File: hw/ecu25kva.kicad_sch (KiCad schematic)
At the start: 0 parts

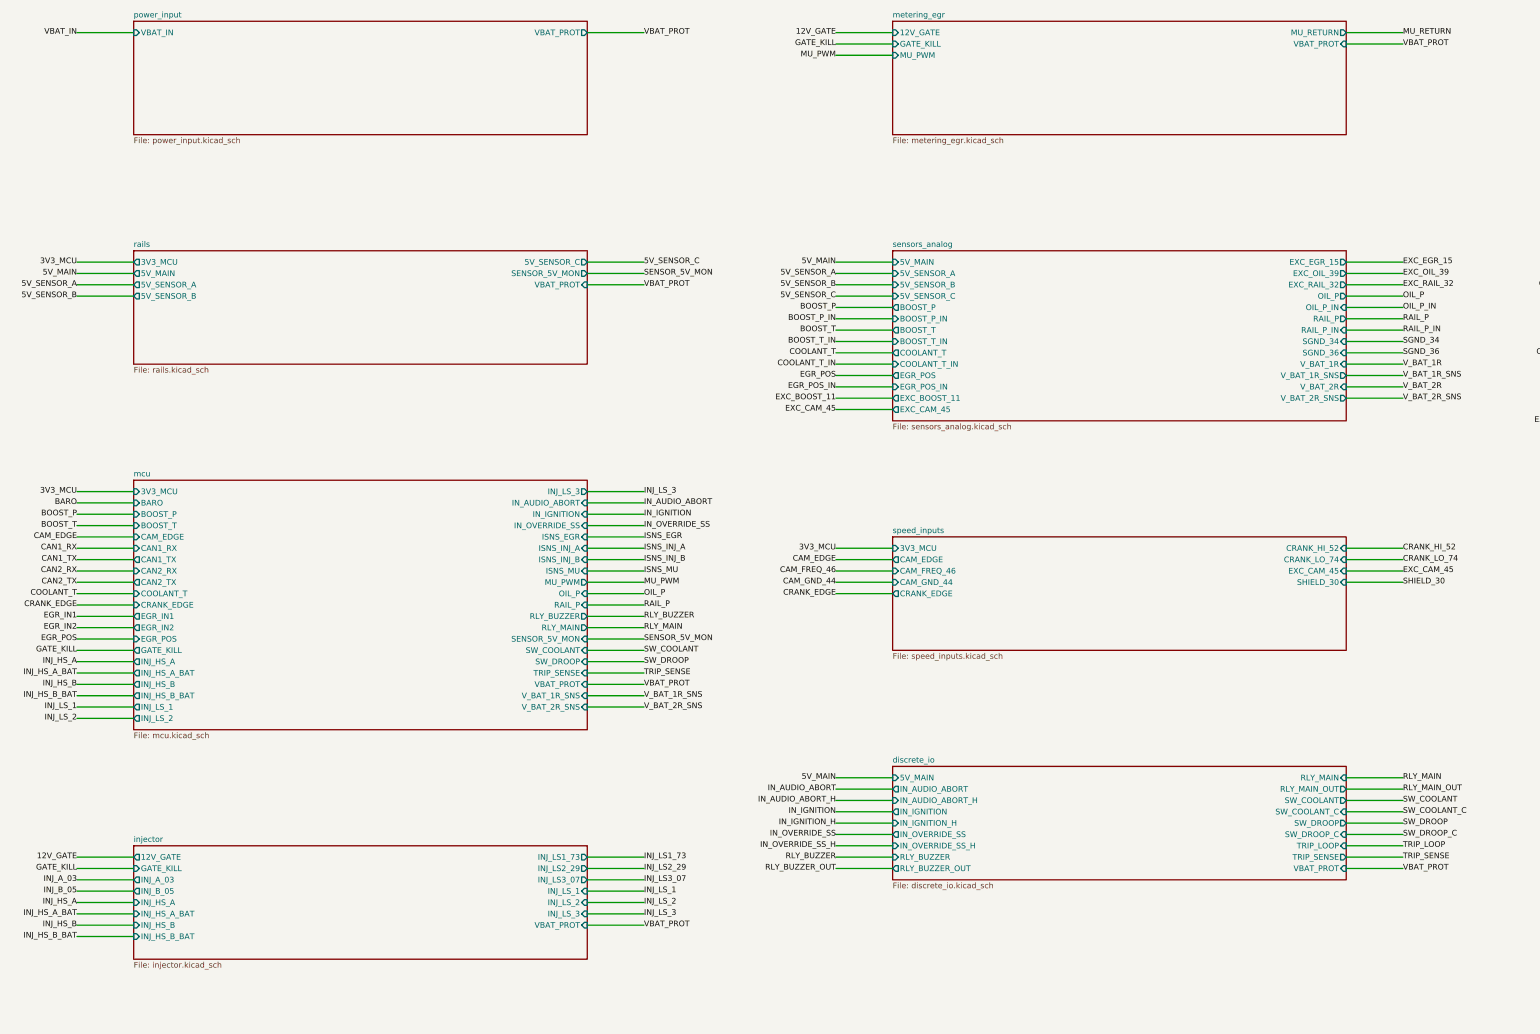
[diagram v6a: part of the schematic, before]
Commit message: Choose the current-sense amplifiers: INA181A1-Q1 on all three channels
TI SLYS018F, retrieved and text-extracted. VCM -0.2 V to 26 V, so it
sits across a ground-referenced shunt; gain 20; 350 kHz; +/-150 uV
offset at VCM = 0.

One part, one gain, three channels, and the gain is set for the
injector: 5 mOhm x 18 A x 20 = 1.80 V at the peak, 1.00 V at the 10 A
hold, leaving headroom to 3.28 V -- so a fault current up to 32.8 A is
MEASURED rather than clipped, which is what an overcurrent check needs.
The metering channel takes the same gain and reads its 0.675 A setpoint
at 675 mV, 844 counts.

Supplied from 3V3_MCU, which makes the output ADC-safe by construction:
it cannot swing above VS - 0.02 V, so these three channels need no
3.3 V zener at the MCU pin, unlike every channel on sensors_analog.

Closes MU-ISENSE's open half -- that tag specified the 50 mOhm shunt and
said the amplifier was not optional. The Kelvin-tap layout requirement
is carried in each amplifier's own field.

Also redrawn: the metering FET, placed at rot=270 since 20 September.
At 270 the drain and source sit side by side and every wire to a rail
above or below comes out diagonal -- the same drawing bug the injector
sheet had and fixed first. The netlist was always right; the page was
not.

Open ends 12 -> 9. 24/24 blocks, 24/24 netlist checks, 36 supply pins
all decoupled.

Co-Authored-By: Claude Opus 5 <noreply@anthropic.com>
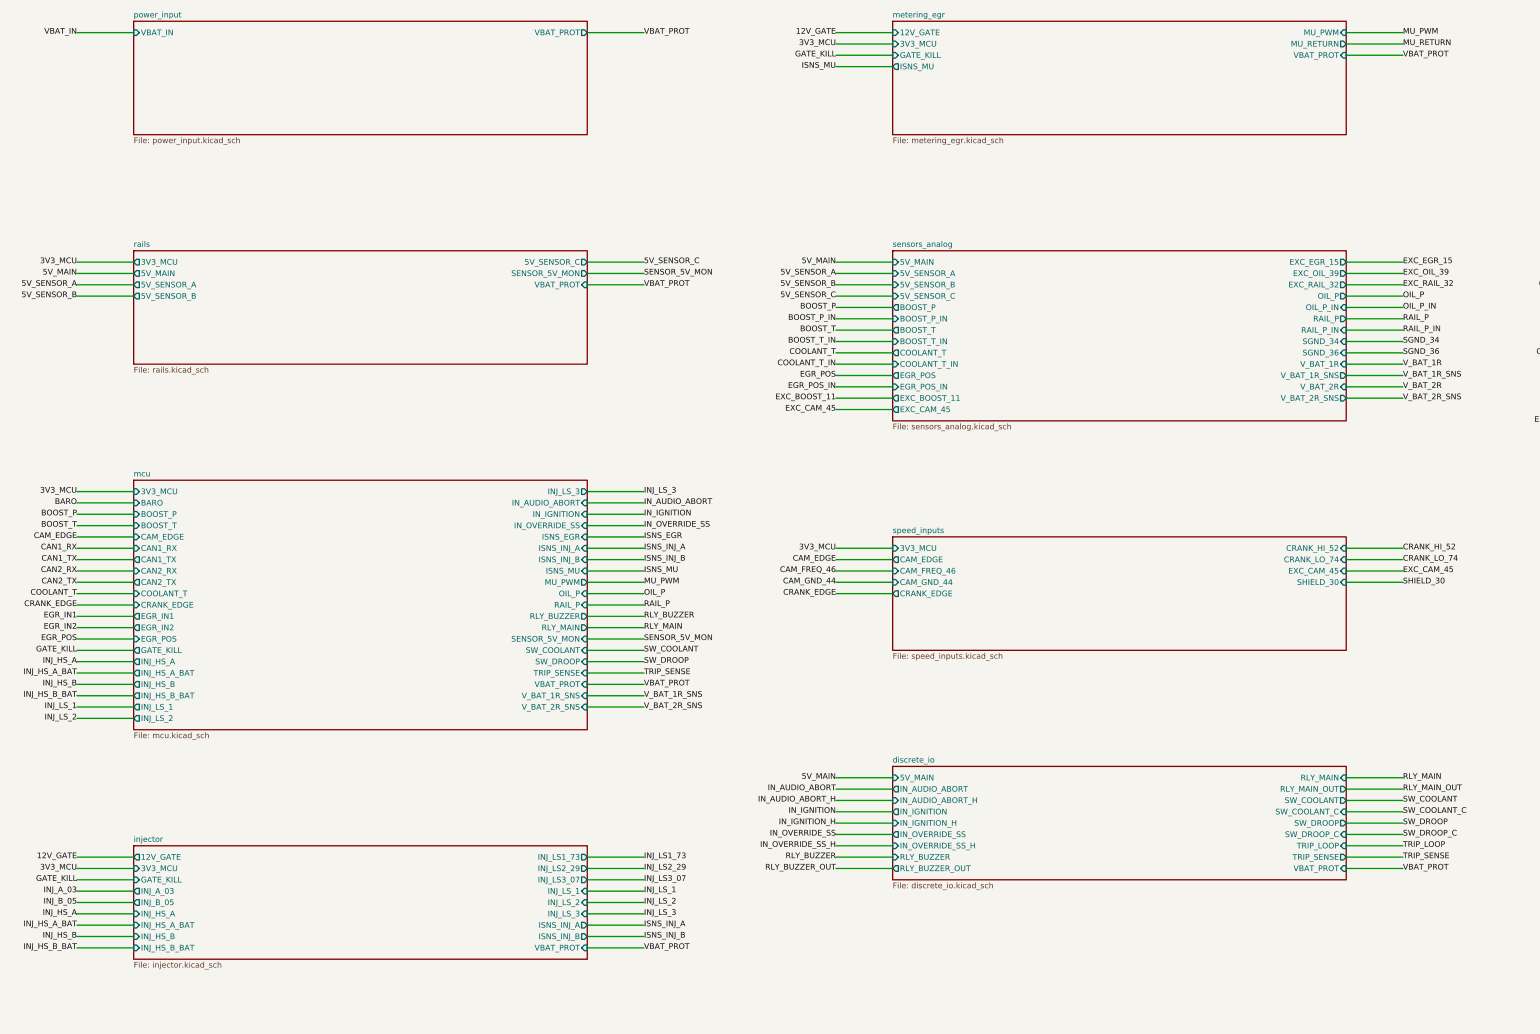
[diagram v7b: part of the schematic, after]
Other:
- sheet injector ports: added 3V3_MCU, ISNS_INJ_A, ISNS_INJ_B; removed none
- sheet metering_egr ports: added 3V3_MCU, ISNS_MU; removed none
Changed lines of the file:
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@@
       (effects (font (size 1.27 1.27)) (justify left))
     )
-    (pin "GATE_KILL" input (at 45.00 217.76 180)
-      (effects (font (size 1.27 1.27)) (justify left))
-    )
-    (pin "INJ_A_03" output (at 45.00 220.30 180)
-      (effects (font (size 1.27 1.27)) (justify left))
-    )
-    (pin "INJ_B_05" output (at 45.00 222.84 180)
-      (effects (font (size 1.27 1.27)) (justify left))
-    )
-    (pin "INJ_HS_A" input (at 45.00 225.38 180)
-      (effects (font (size 1.27 1.27)) (justify left))
-    )
-    (pin "INJ_HS_A_BAT" input (at 45.00 227.92 180)
-      (effects (font (size 1.27 1.27)) (justify left))
-    )
-    (pin "INJ_HS_B" input (at 45.00 230.46 180)
-      (effects (font (size 1.27 1.27)) (justify left))
-    )
-    (pin "INJ_HS_B_BAT" input (at 45.00 233.00 180)
+    (pin "3V3_MCU" input (at 45.00 217.76 180)
+      (effects (font (size 1.27 1.27)) (justify left))
+    )
+    (pin "GATE_KILL" input (at 45.00 220.30 180)
+      (effects (font (size 1.27 1.27)) (justify left))
+    )
+    (pin "INJ_A_03" output (at 45.00 222.84 180)
+      (effects (font (size 1.27 1.27)) (justify left))
+    )
+    (pin "INJ_B_05" output (at 45.00 225.38 180)
+      (effects (font (size 1.27 1.27)) (justify left))
+    )
+    (pin "INJ_HS_A" input (at 45.00 227.92 180)
+      (effects (font (size 1.27 1.27)) (justify left))
+    )
+    (pin "INJ_HS_A_BAT" input (at 45.00 230.46 180)
+      (effects (font (size 1.27 1.27)) (justify left))
+    )
+    (pin "INJ_HS_B" input (at 45.00 233.00 180)
+      (effects (font (size 1.27 1.27)) (justify left))
+    )
+    (pin "INJ_HS_B_BAT" input (at 45.00 235.54 180)
       (effects (font (size 1.27 1.27)) (justify left))
     )
@@
       (effects (font (size 1.27 1.27)) (justify right))
     )
-    (pin "VBAT_PROT" input (at 146.60 230.46 0)
+    (pin "ISNS_INJ_A" output (at 146.60 230.46 0)
+      (effects (font (size 1.27 1.27)) (justify right))
+    )
+    (pin "ISNS_INJ_B" output (at 146.60 233.00 0)
+      (effects (font (size 1.27 1.27)) (justify right))
+    )
+    (pin "VBAT_PROT" input (at 146.60 235.54 0)
       (effects (font (size 1.27 1.27)) (justify right))
     )
@@
       (effects (font (size 1.27 1.27)) (justify left))
     )
-    (pin "GATE_KILL" input (at 215.00 33.08 180)
-      (effects (font (size 1.27 1.27)) (justify left))
-    )
-    (pin "MU_PWM" input (at 215.00 35.62 180)
-      (effects (font (size 1.27 1.27)) (justify left))
-    )
-    (pin "MU_RETURN" output (at 316.60 30.54 0)
-      (effects (font (size 1.27 1.27)) (justify right))
-    )
-    (pin "VBAT_PROT" input (at 316.60 33.08 0)
+    (pin "3V3_MCU" input (at 215.00 33.08 180)
+      (effects (font (size 1.27 1.27)) (justify left))
+    )
+    (pin "GATE_KILL" input (at 215.00 35.62 180)
+      (effects (font (size 1.27 1.27)) (justify left))
+    )
+    (pin "ISNS_MU" output (at 215.00 38.16 180)
+      (effects (font (size 1.27 1.27)) (justify left))
+    )
+    (pin "MU_PWM" input (at 316.60 30.54 0)
+      (effects (font (size 1.27 1.27)) (justify right))
+    )
+    (pin "MU_RETURN" output (at 316.60 33.08 0)
+      (effects (font (size 1.27 1.27)) (justify right))
+    )
+    (pin "VBAT_PROT" input (at 316.60 35.62 0)
       (effects (font (size 1.27 1.27)) (justify right))
     )
@@
     (stroke (width 0) (type default))
   )
-  (label "GATE_KILL" (at 32.30 217.76 180)
+  (label "3V3_MCU" (at 32.30 217.76 180)
     (effects (font (size 1.27 1.27)) (justify right))
   )
@@
     (stroke (width 0) (type default))
   )
-  (label "INJ_A_03" (at 32.30 220.30 180)
+  (label "GATE_KILL" (at 32.30 220.30 180)
     (effects (font (size 1.27 1.27)) (justify right))
   )
@@
     (stroke (width 0) (type default))
   )
-  (label "INJ_B_05" (at 32.30 222.84 180)
+  (label "INJ_A_03" (at 32.30 222.84 180)
     (effects (font (size 1.27 1.27)) (justify right))
   )
@@
     (stroke (width 0) (type default))
   )
-  (label "INJ_HS_A" (at 32.30 225.38 180)
+  (label "INJ_B_05" (at 32.30 225.38 180)
     (effects (font (size 1.27 1.27)) (justify right))
   )
@@
     (stroke (width 0) (type default))
   )
-  (label "INJ_HS_A_BAT" (at 32.30 227.92 180)
+  (label "INJ_HS_A" (at 32.30 227.92 180)
     (effects (font (size 1.27 1.27)) (justify right))
   )
@@
     (stroke (width 0) (type default))
   )
-  (label "INJ_HS_B" (at 32.30 230.46 180)
+  (label "INJ_HS_A_BAT" (at 32.30 230.46 180)
     (effects (font (size 1.27 1.27)) (justify right))
   )
@@
     (stroke (width 0) (type default))
   )
-  (label "INJ_HS_B_BAT" (at 32.30 233.00 180)
+  (label "INJ_HS_B" (at 32.30 233.00 180)
+    (effects (font (size 1.27 1.27)) (justify right))
+  )
+  (wire (pts (xy 45.00 235.54) (xy 32.30 235.54))
+    (stroke (width 0) (type default))
+  )
+  (label "INJ_HS_B_BAT" (at 32.30 235.54 180)
     (effects (font (size 1.27 1.27)) (justify right))
   )
@@
     (stroke (width 0) (type default))
   )
-  (label "VBAT_PROT" (at 159.30 230.46 0)
+  (label "ISNS_INJ_A" (at 159.30 230.46 0)
+    (effects (font (size 1.27 1.27)) (justify left))
+  )
+  (wire (pts (xy 146.60 233.00) (xy 159.30 233.00))
+    (stroke (width 0) (type default))
+  )
+  (label "ISNS_INJ_B" (at 159.30 233.00 0)
+    (effects (font (size 1.27 1.27)) (justify left))
+  )
+  (wire (pts (xy 146.60 235.54) (xy 159.30 235.54))
+    (stroke (width 0) (type default))
+  )
+  (label "VBAT_PROT" (at 159.30 235.54 0)
     (effects (font (size 1.27 1.27)) (justify left))
   )
@@
     (stroke (width 0) (type default))
   )
-  (label "GATE_KILL" (at 202.30 33.08 180)
+  (label "3V3_MCU" (at 202.30 33.08 180)
     (effects (font (size 1.27 1.27)) (justify right))
   )
@@
     (stroke (width 0) (type default))
   )
-  (label "MU_PWM" (at 202.30 35.62 180)
+  (label "GATE_KILL" (at 202.30 35.62 180)
+    (effects (font (size 1.27 1.27)) (justify right))
+  )
+  (wire (pts (xy 215.00 38.16) (xy 202.30 38.16))
+    (stroke (width 0) (type default))
+  )
+  (label "ISNS_MU" (at 202.30 38.16 180)
     (effects (font (size 1.27 1.27)) (justify right))
   )
@@
     (stroke (width 0) (type default))
   )
-  (label "MU_RETURN" (at 329.30 30.54 0)
+  (label "MU_PWM" (at 329.30 30.54 0)
     (effects (font (size 1.27 1.27)) (justify left))
   )
@@
     (stroke (width 0) (type default))
   )
-  (label "VBAT_PROT" (at 329.30 33.08 0)
-    (effects (font (size 1.27 1.27)) (justify left))
-  )
+  (label "MU_RETURN" (at 329.30 33.08 0)
+    (effects (font (size 1.27 1.27)) (justify left))
+  )
+  (wire (pts (xy 316.60 35.62) (xy 329.30 35.62))
+    (stroke (width 0) (type default))
+  )
+  (label "VBAT_PROT" (at 329.30 35.62 0)
+    (effects (font (size 1.27 1.27)) (justify left))
+  )
